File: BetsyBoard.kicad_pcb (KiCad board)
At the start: 4 copper layers, 20.3 x 43.2 mm, 47 parts, among them P1 USB_OTG, P2 Analog, P3 Digital, P5 VIN, P6 CORTEX-JTAG, P7 RTC, P8 BATT, P9 VDD, SW1 RST, SW2 spdp-2x, U1 STM32L486Rx-LQFP64, U2 RClamp0504S, U3 APX823, U4 TPS56x200, U5 N25Q00AA, X1 XTAL, Y1 Crystal

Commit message: More
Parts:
- removed C11: 22uF, smd:SM0805
- removed C14: 0.1uF, smd:SM0603
- removed P1: USB_OTG, engstad:usb-micro-b-amphenol-fci-10118194
- removed R1: 33.2k, smd:SM0603
- removed R2: 10k, smd:SM0603
- removed R6: 10.0k, smd:SM0603
- added J1: USB_OTG, engstad:usb-micro-b-amphenol-fci-10118194, F.Cu at (115.9, 60.0)
- C10, C16: value 10uF -> 1uF
- L1: value 3.3uH -> Bead; footprint engstad:inductor-smd-1212 -> smd:SM0805
- U2: footprint w_smd_trans:sot23-6 -> TO_SOT_Packages_SMD:SOT-23-6
- U4: value TPS56x200 -> LP5907MFX; footprint w_smd_trans:sot23-6 -> TO_SOT_Packages_SMD:SOT-23-5
- moved R7 10.4 mm to (120.9, 63.8)
- moved L1 9.55 mm to (111.6, 65.6)
- moved R5 4.54 mm to (113.9, 71.2)
- moved C10 3.46 mm to (113.4, 65.6), turned to 90 degrees
- moved U4 3.39 mm to (116.0, 65.7), turned to 90 degrees
- moved D3 1.12 mm to (112.4, 71.2), turned to 90 degrees
- moved U2 0.32 mm to (111.8, 66.8), turned to 270 degrees
- moved C20 0.16 mm to (122.6, 63.8)
- moved C12 0.15 mm to (123.0, 86.8)
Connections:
- net /VDDA renamed VDDA
- C10 pad 1: /OTG_5V -> /VIN
- L1 pad 1: /SW -> /OTG_5V
- L1 pad 2: VDD -> /VIN
- U4 pad 1: GND -> /VIN
- U4 pad 2: /SW -> GND
- U4 pad 3: /OTG_5V -> /VIN
- U4 pad 4: /FB -> Net-(U4-Pad4)
- U4 pad 5: /EN -> VDD
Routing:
- net Earth: track 15.7 -> 5.64 mm
- net VDD: track 87.5 -> 80.6 mm, vias 8 -> 7
- net /VIN: track 0.00 -> 6.64 mm
- net /OTG_5V: track 39.7 -> 46.3 mm, vias 5 -> 3
- net /SW: track 5.58 -> 0.00 mm
- net /FB: track 4.39 -> 0.00 mm
- net /EN: track 3.53 -> 0.00 mm
- net GND: track 48.4 -> 46.7 mm
- net Net-(C14-Pad1): track 1.63 -> 0.00 mm
- net Net-(D3-Pad1): track 2.23 -> 1.48 mm
- net /OTG_FS_D-: track 34.4 -> 33.8 mm
- removed copper zone on B.Cu, net /OTG_5V
- removed copper zone on B.Cu, net /SW
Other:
- board text added: "BetsyBoard V0.8"
- board text removed: "BetsyBoard V0.7"

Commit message: small dabbles
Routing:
- net /OTG_5V: track 46.3 -> 40.4 mm, vias 3 -> 4
- net GND: track 46.7 -> 48.6 mm, vias 11 -> 12

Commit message: apx comments
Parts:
- renumbered C10 to C1, C18 to C10, C12 to C11, C2 to C12, C3 to C13, C5 to C14, C6 to C15, C7 to C16, C8 to C17, C16 to C2, C15 to C3, C20 to C4, C4 to C5, C9 to C6, C1 to C7, C17 to C8, C19 to C9, D3 to D2, L3 to L2, P5 to P1, P9 to P2, P6 to P3, P2 to P4, P3 to P5, P8 to P6, R7 to R1, R4 to R2, R5 to R4, SW2 to SW1, SW1 to SW2, U4 to U1, U1 to U4
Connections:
- P3 pad 7: Net-(P6-Pad7) -> (no net)
- U1 pad 4: Net-(U4-Pad4) -> (no net)
- U2 pad 6: Net-(U2-Pad6) -> (no net)
- U3 pad 4: Net-(U3-Pad4) -> (no net)

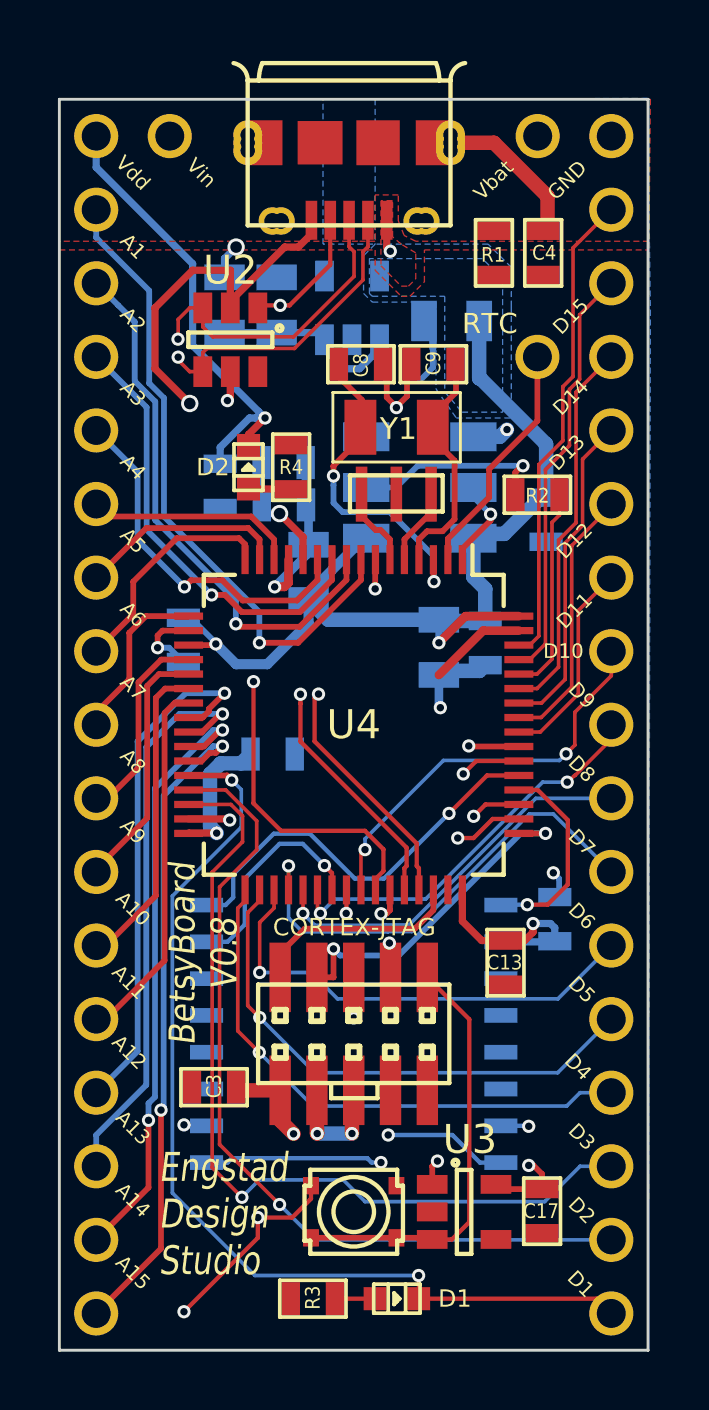
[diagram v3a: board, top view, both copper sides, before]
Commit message: Working towards 0.9.
- Remove NJTRST and NRST confusion
- Remove VBUS, not needed for upstream facing port.
- Remove shielding, don't mess with the upstream ground.
- Put back SDMMC, it's not the same as QSPI.
- Add README.md.
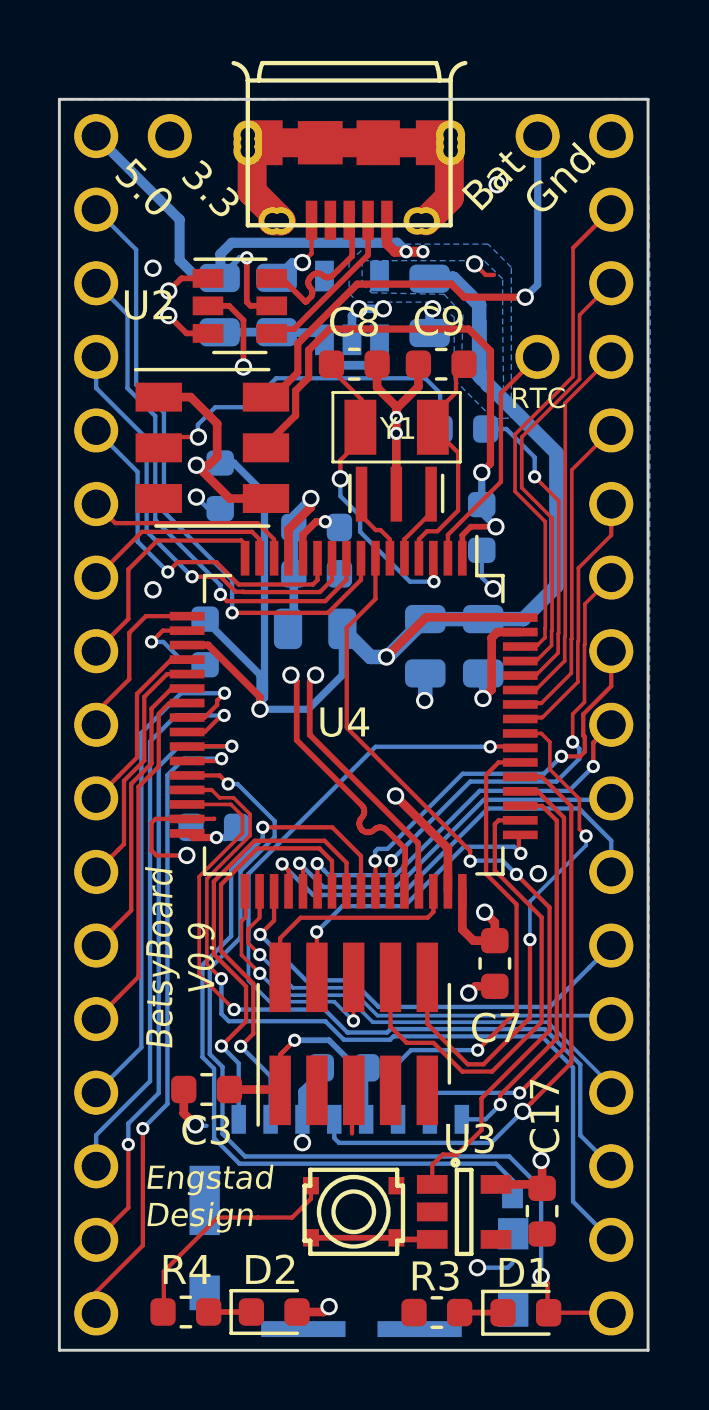
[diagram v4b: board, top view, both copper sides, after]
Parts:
- removed C4: 4.7uF, smd:SM0603
- removed L1, L2: Bead, smd:SM0805
- removed R1: 1M0, smd:SM0603
- removed U5: N25Q00AA, SMD_Packages:SO-16-W
- added FB1: 220Ω@100MHz, Inductor_SMD:L_0805_2012Metric, B.Cu at (111.4, 65.6)
- added FB2: 220Ω@100MHz, Inductor_SMD:L_0805_2012Metric, B.Cu at (114.7, 76.8)
- added J2: Micro_SD_Card, engstad:Molex_PS_105162_001, B.Cu at (116.2, 97.2)
- C1, C12, C2: footprint smd:SM0805 -> Capacitor_SMD:C_0805_2012Metric
- C10, C11, C14, C15, C16, C17, C3, C5, C6, C8, C9: footprint smd:SM0603 -> Capacitor_SMD:C_0603_1608Metric
- C13: footprint smd:SM0603 -> Capacitor_SMD:C_0805_2012Metric; moved to B.Cu
- C7: footprint smd:SM0603 -> Capacitor_SMD:C_0603_1608Metric; moved to F.Cu
- D1, D2: footprint w_smd_leds:Led_0603 -> LED_SMD:LED_0603_1608Metric
- J1: value USB_OTG -> USB_B_Micro
- P1: value VIN -> VDD
- P2: value VDD -> VBUS
- R2: footprint smd:SM0603 -> Resistor_SMD:R_0603_1608Metric; moved to B.Cu
- R3, R4: footprint smd:SM0603 -> Resistor_SMD:R_0603_1608Metric
- SW1: moved to F.Cu
- U2: value RClamp0504S -> USBLC6-2SC6; footprint TO_SOT_Packages_SMD:SOT-23-6 -> Package_TO_SOT_SMD:SOT-23-6
- U4: footprint Housings_QFP:LQFP-64_10x10mm_Pitch0.5mm -> engstad:QFP-64_10x10_Pitch0.5mm
- moved R4 29.4 mm to (110.2, 100.3), turned to 180 degrees
- moved D2 29.2 mm to (113.3, 100.3), turned to 0 degrees
- moved C15 11.3 mm to (111.2, 83.6), turned to 180 degrees
- moved C13 11.3 mm to (118.5, 77.3)
- moved C7 10.5 mm to (120.9, 88.3), turned to 90 degrees
- moved C11 8.90 mm to (115.7, 91.9), turned to 180 degrees
- moved SW1 7.29 mm to (111.2, 70.5), turned to 270 degrees
- moved D1 4.48 mm to (122.0, 100.4)
- moved R3 4.31 mm to (118.9, 100.3)
- moved R2 3.43 mm to (119.8, 69.8)
- moved C6 2.63 mm to (114.8, 74.8), turned to 0 degrees
- moved C5 2.51 mm to (114.8, 73.2), turned to 0 degrees
- moved C10 2.24 mm to (120.5, 73.2)
- moved C12 1.53 mm to (120.5, 77.3)
- moved U2 1.22 mm to (112.1, 65.6), turned to 0 degrees
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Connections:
- C10 pad 1: VDD -> /VBAT
- J1 pad 1: /OTG_5V -> /VBUS
- J1 pad 2: /OTG_FS_D- -> /D-
- J1 pad 3: /OTG_FS_D+ -> /D+
- J1 pad 4: /OTG_FS_ID -> Net-(J1-Pad4)
- J1 pad 6: Earth -> Net-(J1-Pad6)
- P1 pad 1: /OTG_5V -> VDD
- P2 pad 1: VDD -> /VBUS
- P3 pad 10: /~MR -> /~JTRST
- P3 pad 7: (no net) -> Net-(P3-Pad7)
- SW1 pad 4: VDD -> /VBAT_IN
- SW1 pad 6: /VBAT_IN -> VDD
- SW2 pad 2: /~MR -> Net-(SW2-Pad2)
- U1 pad 4: (no net) -> Net-(U1-Pad4)
- U2 pad 1: /OTG_FS_ID -> /OTG_FS_D+
- U2 pad 3: /OTG_FS_D+ -> /OTG_FS_D-
- U2 pad 4: /OTG_FS_D- -> /D-
- U2 pad 5: /OTG_5V -> /VBUS
- U2 pad 6: (no net) -> /D+
- U3 pad 3: /~MR -> Net-(SW2-Pad2)
- U3 pad 4: (no net) -> Net-(U3-Pad4)
- U4 pad 41: /D10 -> /SDMMC_DET
- U4 pad 42: /OTG_5V -> /D10
- U4 pad 43: /OTG_FS_ID -> /D11
- U4 pad 56: /D11 -> /~JTRST
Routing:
- net /OTG_5V: track 40.4 -> 0.00 mm, vias 4 -> 0
- net /OTG_FS_ID: track 28.6 -> 0.00 mm, vias 2 -> 0
- net /SDMMC_DET: track 0.00 -> 28.3 mm, vias 0 -> 1
- net /VBUS: track 0.00 -> 20.5 mm, vias 0 -> 3
- net /~JTRST: track 0.00 -> 18.4 mm, vias 0 -> 2
- net /VBAT: track 3.29 -> 19.6 mm, vias 1 -> 2
- net /~MR: track 14.8 -> 0.00 mm
- net Net-(J1-Pad6): track 0.00 -> 12.7 mm
- net /SDMMC_D3: track 6.95 -> 15.9 mm
- net /D11: track 7.08 -> 15.9 mm, vias 0 -> 2
- net /JTDI: track 8.79 -> 17.3 mm, vias 2 -> 0
- net VDD: track 80.6 -> 89.0 mm, vias 7 -> 8
- net GND: track 48.6 -> 56.6 mm, vias 12 -> 24
- net /SDMMC_D2: track 21.3 -> 13.6 mm, vias 2 -> 1
- net /OTG_FS_D+: track 34.7 -> 27.4 mm
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- removed copper zone on F.Cu, net /OTG_5V
- removed copper zone on Pow.Cu, net /OTG_5V
- removed copper zone on F.Cu, net Earth
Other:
- net class PowerMain added: clearance 0.2, trace_width 0.3, via_dia 0.6, via_drill 0.4
- board text added: "3.3"
- board text added: "5.0"
- board text added: "Bat"
- board text added: "BetsyBoard V0.9"
- board text added: "D16"
- board text added: "Engstad Design"
- board text added: "Gnd"
- board text removed: "10"
- board text removed: "11"
- board text removed: "12"
- board text removed: "13"
- board text removed: "3"
- board text removed: "6"
- board text removed: "7"
- board text removed: "A14"
- board text removed: "A15"
- board text removed: "BetsyBoard V0.8"
- board text removed: "D14"
- board text removed: "Engstad Design Studio"
- board text removed: "Vbat"
- board text removed: "Vdd"
- board text removed: "Vin"

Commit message: More changes
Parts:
- added NT1: Net-Tie_2, NetTie:NetTie-2_SMD_Pad0.5mm, F.Cu at (115.2, 72.4)
- SW1: value spdp-2x -> DIPSW
- U1: value LP5907MFX -> LP5907MFX-3.3; footprint TO_SOT_Packages_SMD:SOT-23-5 -> Package_TO_SOT_SMD:SOT-23-5
- U3: footprint TO_SOT_Packages_SMD:SOT-23-5 -> Package_TO_SOT_SMD:SOT-23-5
- Y1: footprint armory:CRYSTAL-32k-B -> Crystal:Crystal_SMD_3215-2Pin_3.2x1.5mm
- moved C1 0.22 mm to (113.2, 65.6)
- moved FB1 0.20 mm to (111.2, 65.6)
- moved C2 0.15 mm to (118.8, 65.6)
- moved J2 0.07 mm to (116.2, 97.2), turned to 180 degrees
- turned Y1 to 180 degrees
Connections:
- U4 pad 12: GND -> VSSA
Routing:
- net /SDMMC_D2: track 13.6 -> 27.2 mm
- net GND: track 56.6 -> 43.0 mm, vias 24 -> 22
- net /SDMMC_D1: track 15.7 -> 28.5 mm
- net /SDMMC_CMD: track 16.7 -> 28.6 mm, vias 1 -> 5
- net /SDMMC_D0: track 14.7 -> 26.5 mm
- net /SDMMC_D3: track 15.9 -> 26.9 mm
- net VDD: track 89.0 -> 99.7 mm, vias 8 -> 12
- net /SDMMC_DET: track 28.3 -> 21.5 mm
- net /RTC_OSC_IN: track 10.2 -> 13.0 mm
- net /SDMMC_CLK: track 21.1 -> 23.9 mm
- net /VBAT_IN: track 17.4 -> 14.8 mm, vias 1 -> 0
- net /BOOT_SEL: track 12.3 -> 9.89 mm
- net /~JTRST: track 18.4 -> 16.1 mm, vias 2 -> 0
- net /RTC_OSC_OUT: track 8.01 -> 10.1 mm
- net VSSA: track 0.00 -> 1.97 mm
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- removed copper zone on Pow.Cu, net /VBAT_IN

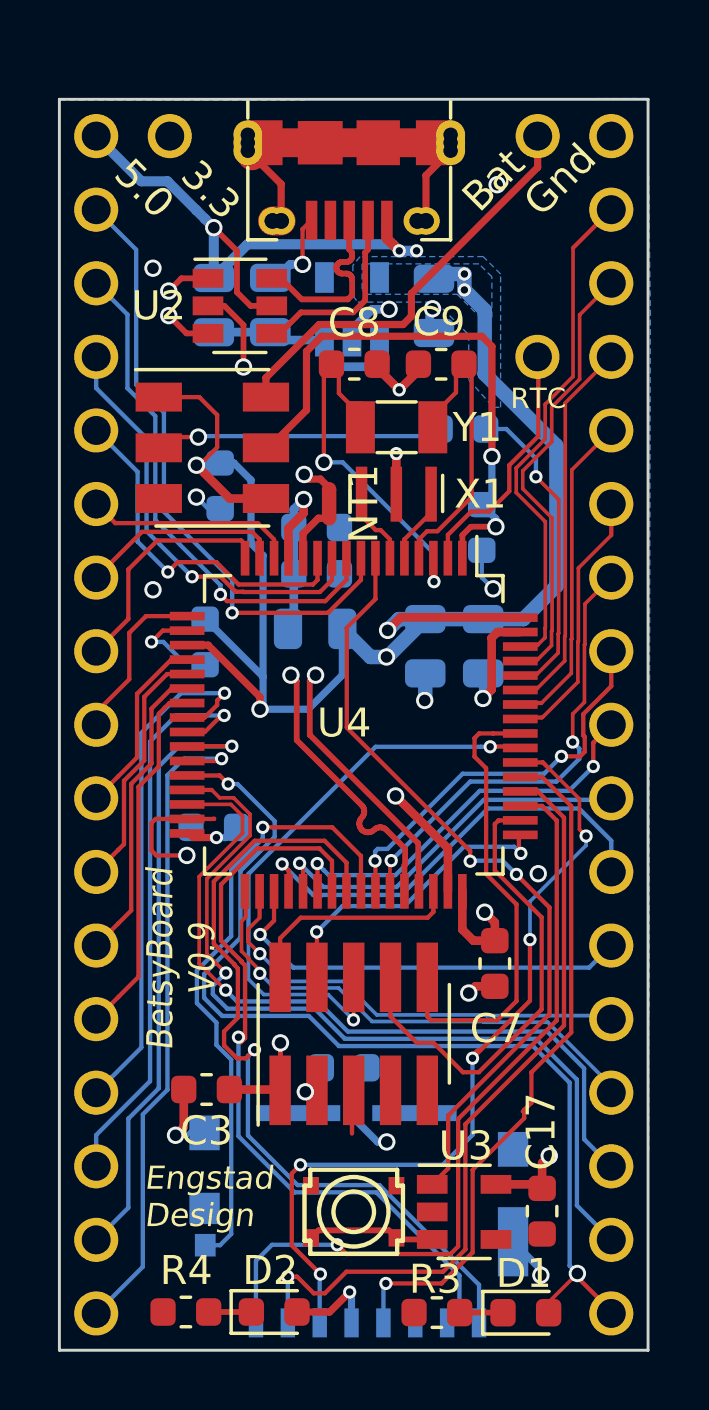
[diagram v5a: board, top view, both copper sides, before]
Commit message: Major changes due to mistakes
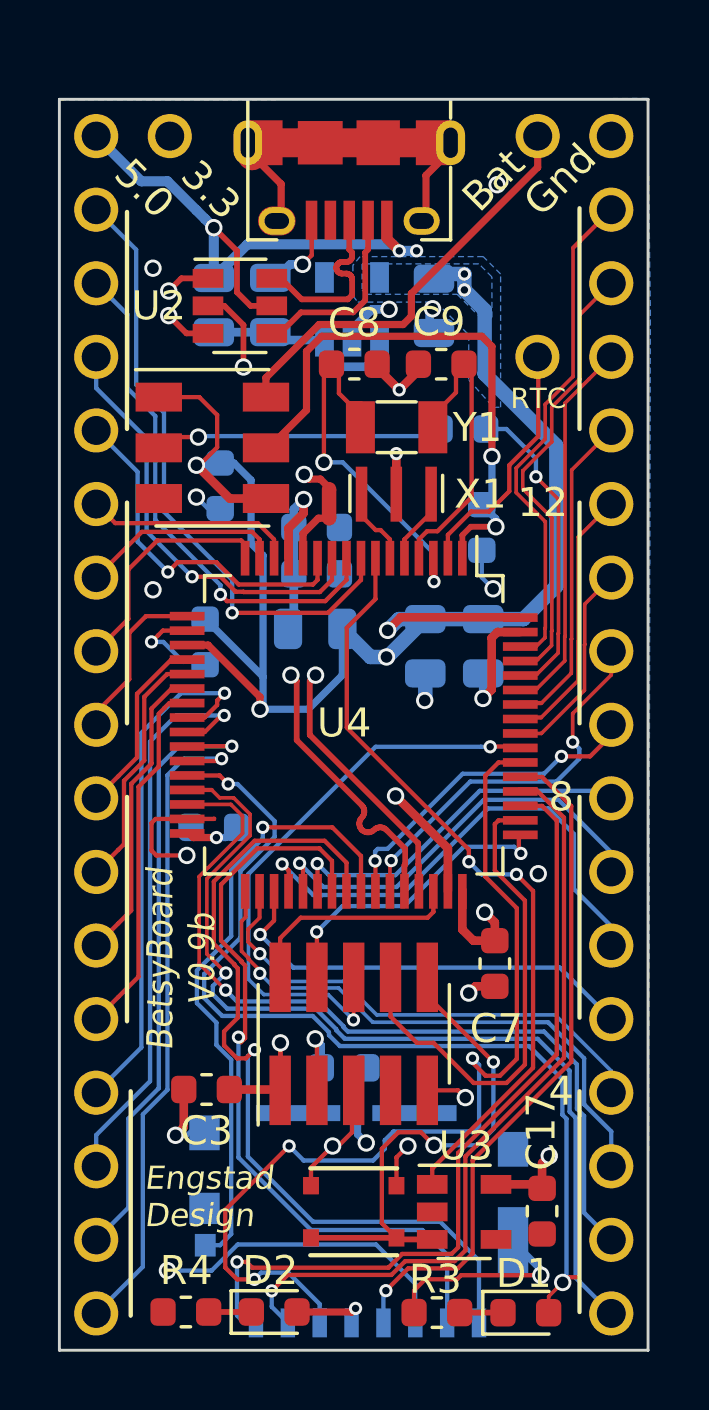
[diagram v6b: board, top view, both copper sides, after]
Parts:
- J1: footprint engstad:usb-micro-b-amphenol-fci-10118194 -> engstad:usb-micro-b-amphenol-fci-10118194-oval
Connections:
- D1 pad 2: /D1 -> /LED
- P3 pad 10: /~JTRST -> /RESET#
- SW2 pad 2: Net-(SW2-Pad2) -> /RESET#
- U3 pad 3: Net-(SW2-Pad2) -> /RESET#
- U4 pad 28: /D1 -> /LED
- U4 pad 29: /D2 -> /D1
- U4 pad 30: /D3 -> /D2
- U4 pad 33: /D4 -> /D3
- U4 pad 34: /D5 -> /D4
- U4 pad 35: /D6 -> /D5
- U4 pad 36: /D7 -> /D6
- U4 pad 37: /D8 -> /D7
- U4 pad 38: /D9 -> /D8
- U4 pad 42: /D10 -> /D9
- U4 pad 43: /D11 -> /D10
- U4 pad 56: /~JTRST -> /D11
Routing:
- net /LED: track 0.00 -> 33.6 mm, vias 0 -> 2
- net GND: track 43.0 -> 66.3 mm, vias 22 -> 26
- net /RESET#: track 0.00 -> 18.2 mm, vias 0 -> 2
- net /~JTRST: track 16.1 -> 0.00 mm
- net /D11: track 15.9 -> 7.11 mm, vias 2 -> 0
- net /D3: track 26.2 -> 19.7 mm
- net /SDMMC_CMD: track 28.6 -> 33.4 mm, vias 5 -> 3
- net Net-(SW2-Pad2): track 4.42 -> 0.00 mm
- net /D1: track 35.3 -> 32.2 mm, vias 2 -> 1
- net /D6: track 14.6 -> 17.5 mm
- net /D9: track 13.9 -> 11.6 mm
- net /SDMMC_D2: track 27.2 -> 28.2 mm
- net VDD: track 99.7 -> 98.7 mm
- net /SDMMC_D1: track 28.5 -> 29.4 mm
- net /D2: track 29.6 -> 28.7 mm
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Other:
- board text added: "12"
- board text added: "4"
- board text added: "8"
- board text added: "BetsyBoard V0.9b"
- board text removed: "BetsyBoard V0.9"

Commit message: Version 0.9c of BetsyBoard
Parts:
- removed FB1: 220Ω@100MHz, Inductor_SMD:L_0805_2012Metric
- removed SW1: DIPSW, engstad:slide-switch-smd-cas-220-d20
- added C18: 10pF, Capacitor_SMD:C_0603_1608Metric, F.Cu at (114.7, 71.3)
- added C4: 10pF, Capacitor_SMD:C_0603_1608Metric, F.Cu at (120.3, 71.3)
- added F1: Fuse_Small, Fuse:Fuse_0805_2012Metric, B.Cu at (111.2, 65.6)
- NT1: footprint NetTie:NetTie-2_SMD_Pad0.5mm -> engstad:net-tie-0.4mm
- P6: value BATT -> VDD; footprint engstad:pin-socket-2 -> Connector_PinHeader_2.54mm:PinHeader_1x01_P2.54mm_Vertical
- P7: value RTC -> MCO
- moved P7 7.62 mm to (122.4, 59.7)
- moved NT1 2.91 mm to (112.7, 71.0), turned to 0 degrees
- moved P6 1.27 mm to (124.9, 59.7)
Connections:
- C10 pad 1: /VBAT -> VDD
- P6 pad 1: /VBAT_IN -> GND
- P7 pad 1: /RTC -> /MCO
- R2 pad 1: /BOOT_SEL -> GND
- U4 pad 1: /VBAT -> VDD
- U4 pad 2: /RTC -> /SDMMC_DET
- U4 pad 41: /SDMMC_DET -> /MCO
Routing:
- net /MCO: track 0.00 -> 31.1 mm, vias 0 -> 1
- net /VBAT: track 19.8 -> 0.00 mm, vias 2 -> 0
- net /VBAT_IN: track 14.8 -> 0.00 mm
- net /BOOT_SEL: track 9.89 -> 0.00 mm, vias 1 -> 0
- net /RTC: track 8.61 -> 0.00 mm
- net /SDMMC_DET: track 21.5 -> 29.5 mm, vias 1 -> 3
- net GND: track 66.3 -> 73.9 mm, vias 26 -> 27
- net /SDMMC_CMD: track 33.4 -> 36.0 mm
- net VSSA: track 1.97 -> 3.79 mm
- net VDDA: track 6.93 -> 8.65 mm
- net /OSC_IN: track 2.64 -> 4.25 mm
- net /OSC_OUT: track 2.77 -> 4.38 mm
- net /RTC_OSC_OUT: track 10.1 -> 11.6 mm
- net /SDMMC_D0: track 26.5 -> 27.8 mm
- net VDD: track 98.7 -> 97.5 mm
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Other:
- rule pad_to_mask_clearance: 0.05 -> 0
- board text added: "BetsyBoard V0.9c"
- board text added: "JLCJLCJLCJLC"
- board text added: "MCO"
- board text removed: "Bat"
- board text removed: "BetsyBoard V0.9b"
- board text removed: "RTC"

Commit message: More work on battery charging.
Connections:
- net /~RST renamed /~{RST}
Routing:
- added copper zone on In1.Cu, net GND
- added copper zone on In2.Cu, net GND
- added copper zone on In2.Cu, net VDD
- removed copper zone on Gnd.Cu, net GND
- removed copper zone on Pow.Cu, net GND
- removed copper zone on Pow.Cu, net VDD
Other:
- net class Default removed
- net class PowerMain removed
- net class USB removed
